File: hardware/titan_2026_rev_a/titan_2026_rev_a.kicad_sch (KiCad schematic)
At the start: 29 parts, among them J1 DS1023-2*20SF11, J6 HB-PH9-12727PB2GOB, J9 USB4105-GF-A-120, SW1 SW_SPST, U3 STM32F105RCT6, U5 USBLC6-2SC6, Y1 8M

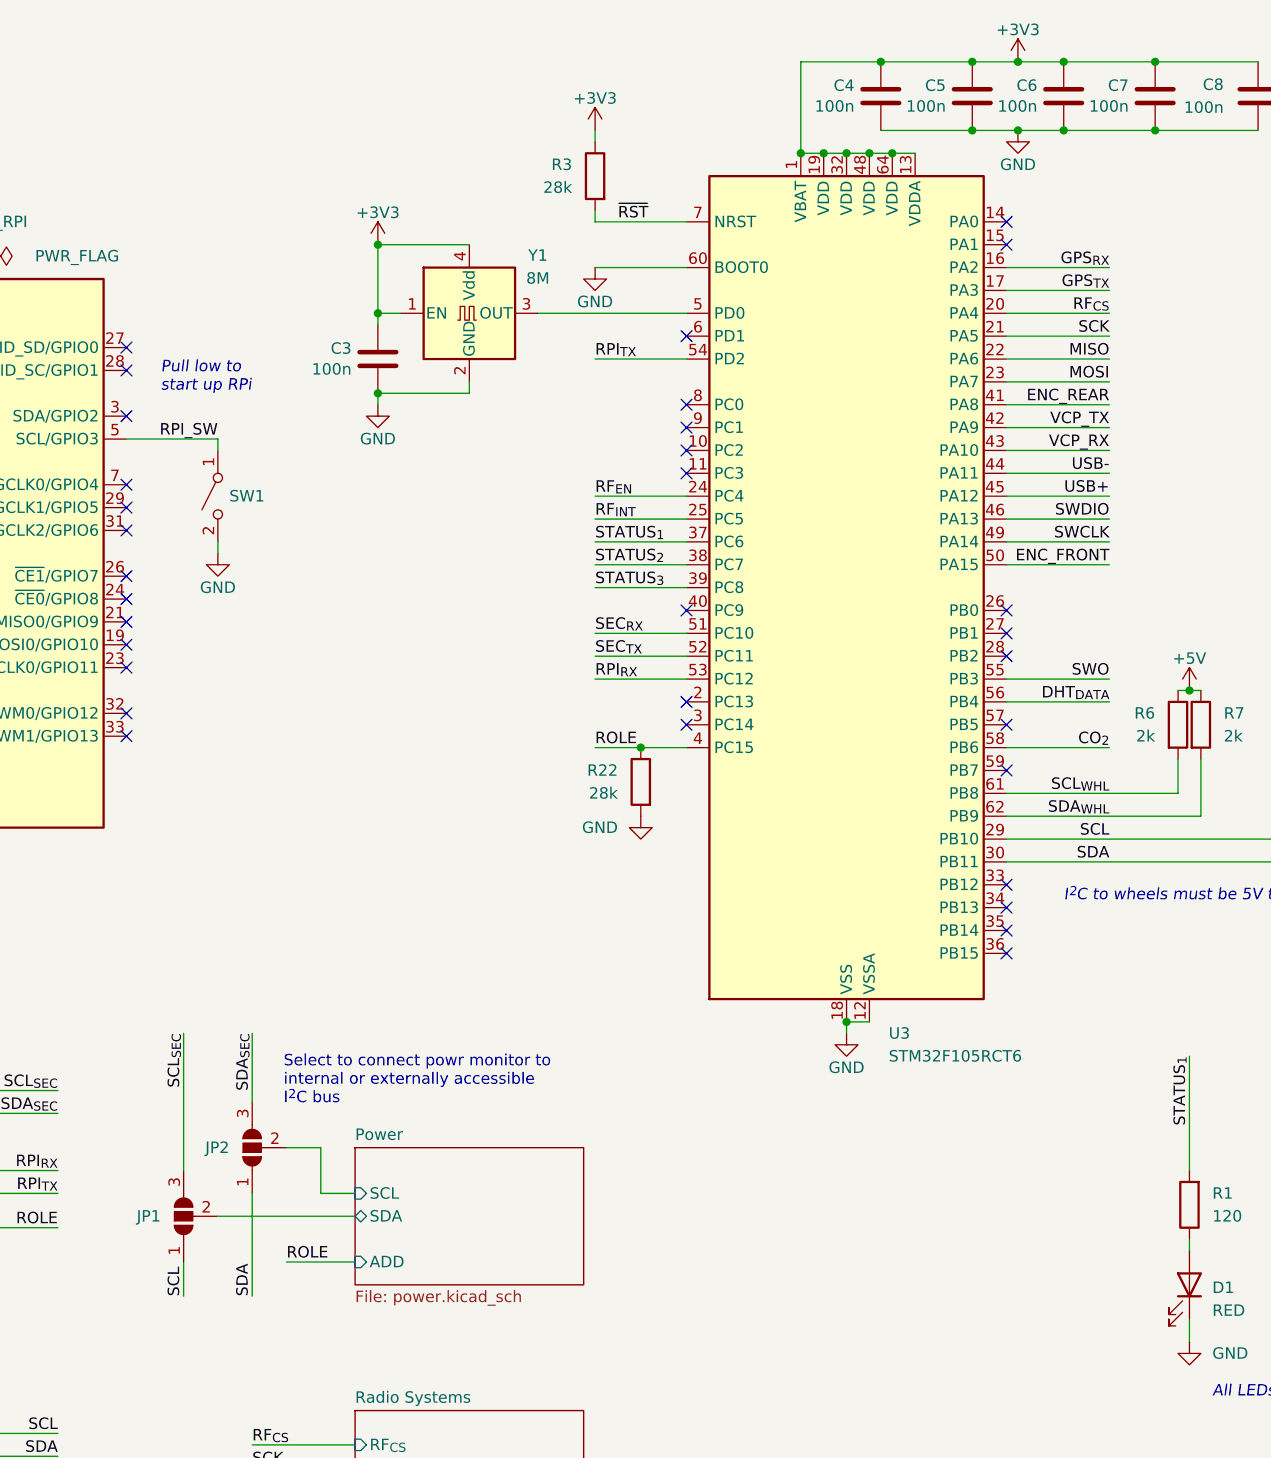
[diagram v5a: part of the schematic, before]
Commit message: Juggled some connections for routing
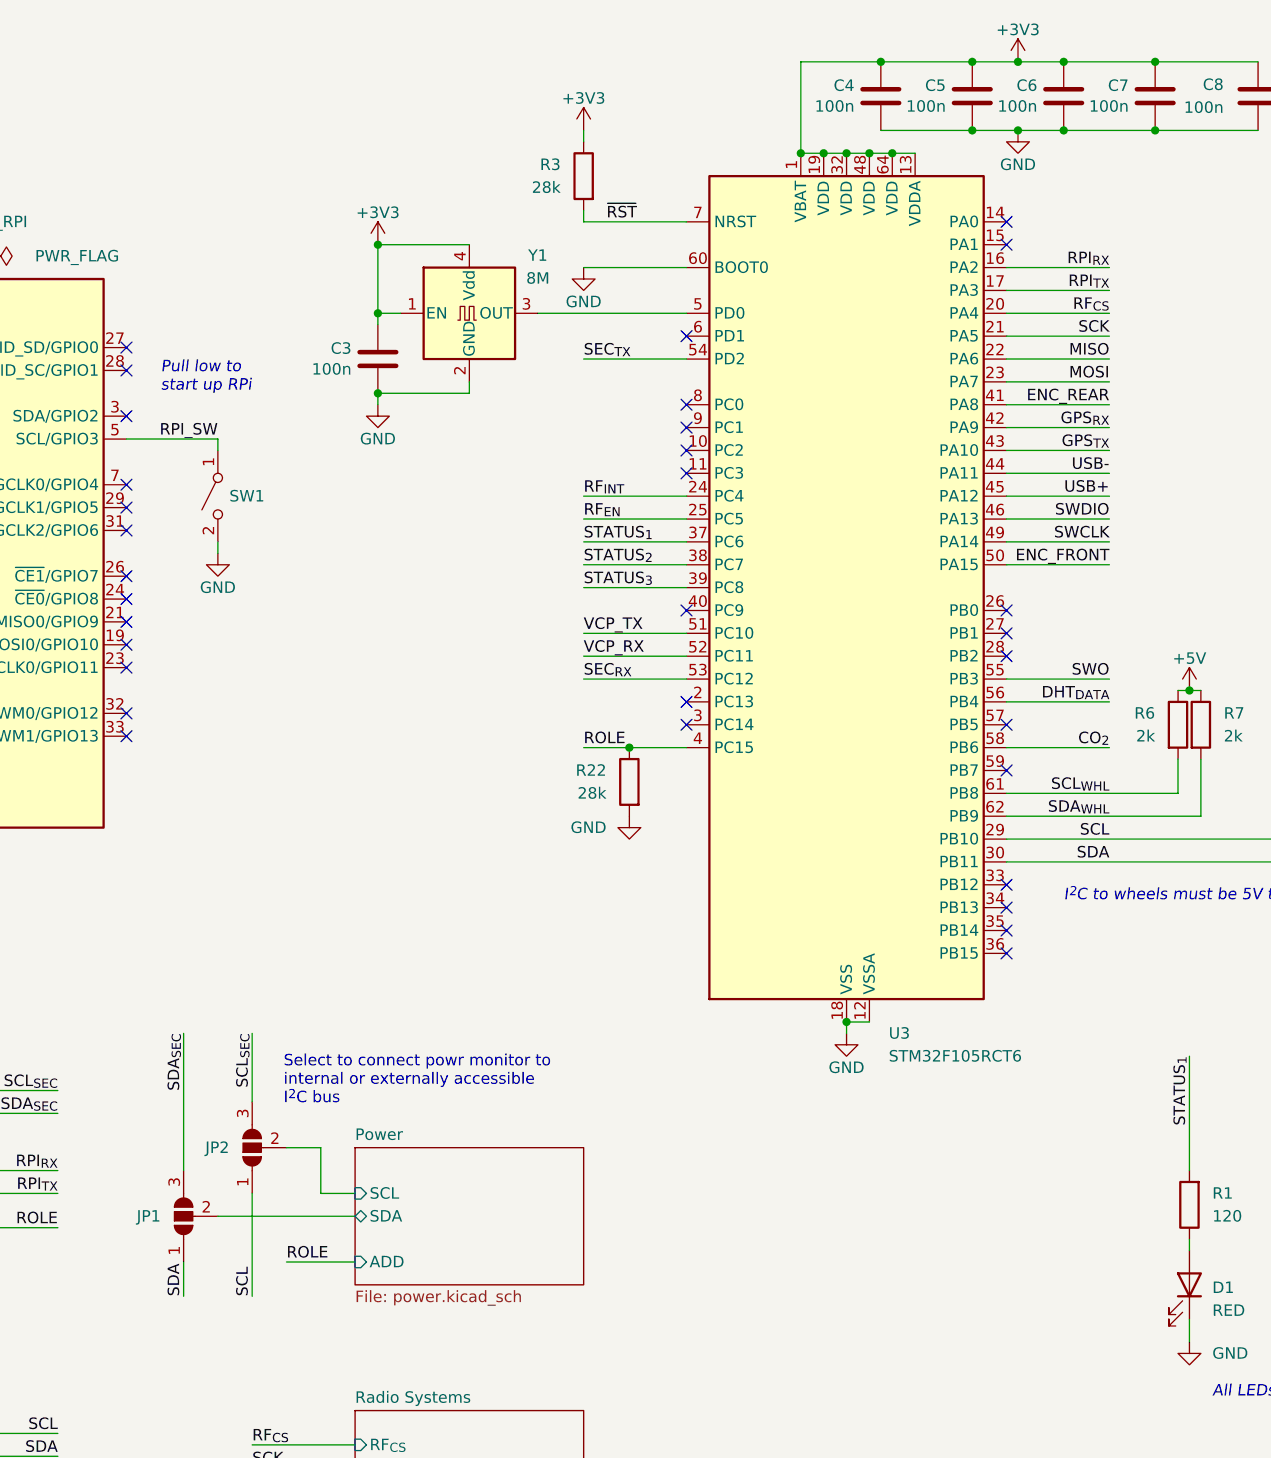
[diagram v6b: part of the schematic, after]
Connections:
- net GPS_{RX}: now also U3.42 (PA9); no longer U3.16 (PA2)
- net GPS_{TX}: now also U3.43 (PA10); no longer U3.17 (PA3)
- net RF_{EN}: now also U3.25 (PC5); no longer U3.24 (PC4)
- net RF_{INT}: now also U3.24 (PC4); no longer U3.25 (PC5)
- net RPI_{RX}: now also U3.16 (PA2); no longer U3.53 (PC12)
- net RPI_{TX}: now also U3.17 (PA3); no longer U3.54 (PD2)
- net SCL: now also JP2.1 (A); no longer JP1.1 (A)
- net SCL_{SEC}: now also JP2.3 (B); no longer JP1.3 (B)
- net SDA: now also JP1.1 (A); no longer JP2.1 (A)
- net SDA_{SEC}: now also JP1.3 (B); no longer JP2.3 (B)
- net SEC_{RX}: now also U3.53 (PC12); no longer U3.51 (PC10)
- net SEC_{TX}: now also U3.54 (PD2); no longer U3.52 (PC11)
- net VCP_RX: now also U3.52 (PC11); no longer U3.43 (PA10)
- net VCP_TX: now also U3.51 (PC10); no longer U3.42 (PA9)
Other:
- moved on the sheet: R22, R3

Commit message: HAT Rev. A ready for ordering
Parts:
- removed R6, R7: 2k, Resistor_SMD:R_0402_1005Metric, symbol Device:R
